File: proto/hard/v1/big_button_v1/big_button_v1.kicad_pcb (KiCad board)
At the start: 2 copper layers, 20 x 50 mm, 18 parts, among them J1 RJ12, J2 RJ12, J3 Conn_01x02, J4 Conn_01x02, SW1 SW_Push, U1 LM393, U2 PC817, U3 PC817

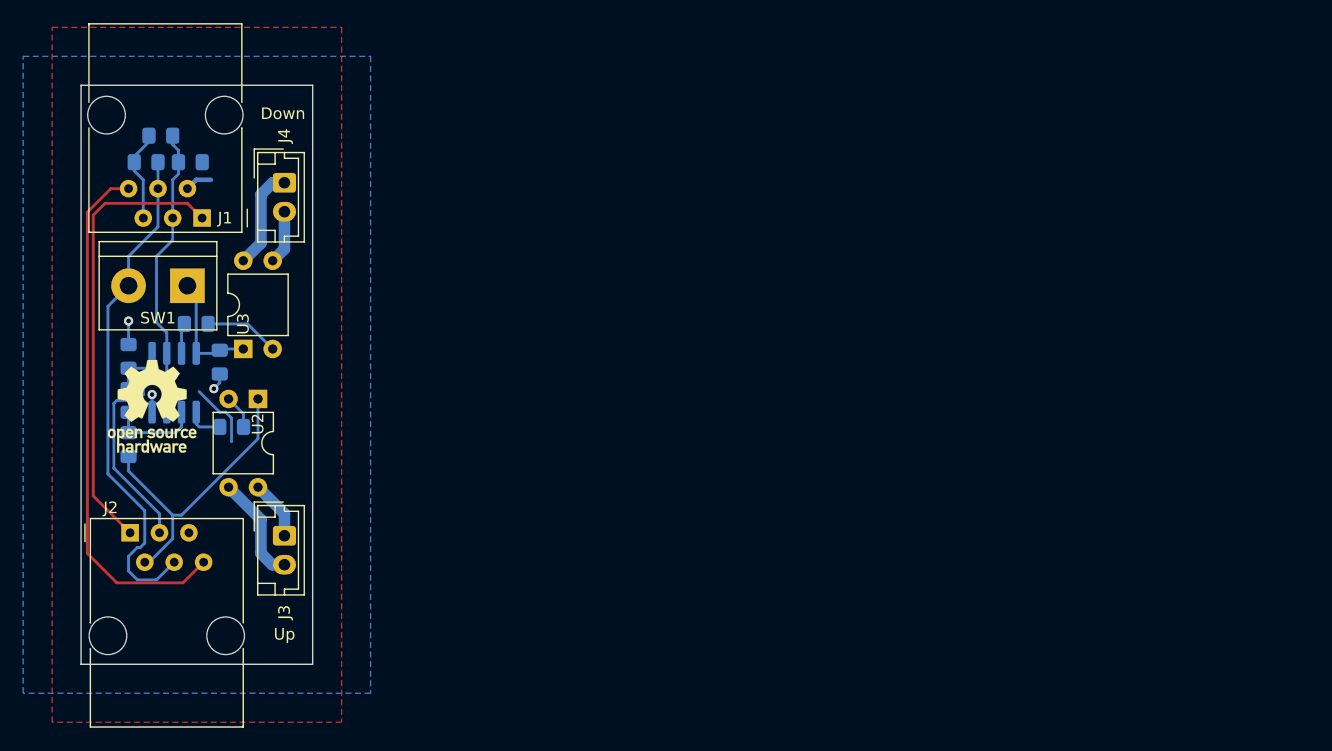
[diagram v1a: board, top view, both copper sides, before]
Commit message: Button rework - specialization for small case BMW50028. Includes button and single click LED highlight. Added diode to power line. Changed to single comparator.
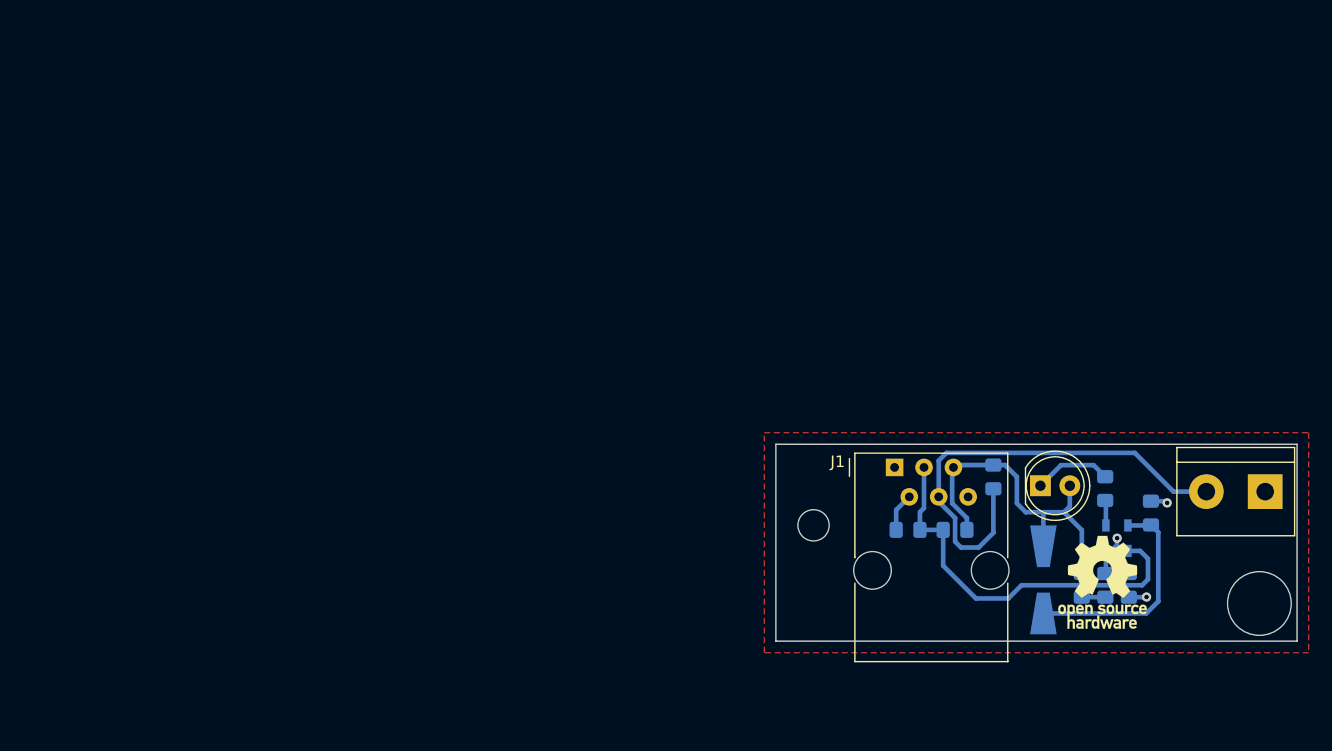
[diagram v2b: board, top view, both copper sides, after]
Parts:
- removed J2: RJ12, Connector_RJ:RJ12_Amphenol_54601
- removed J3, J4: Conn_01x02, Connector_JST:JST_EH_B2B-EH-A_1x02_P2.50mm_Vertical
- removed R8: 1k, Resistor_SMD:R_0805_2012Metric_Pad1.15x1.40mm_HandSolder
- removed U2, U3: PC817, Package_DIP:DIP-4_W7.62mm
- added D1: D_Schottky, Diode_SMD:D_SMA-SMB_Universal_Handsoldering, B.Cu at (133.1, 92.7)
- added D2: LED, LED_THT:LED_D5.0mm, F.Cu at (132.8, 84.6)
- added REF**: MountingHole_5.5mm, MountingHole:MountingHole_5.5mm, F.Cu at (151.8, 94.8)
- added REF**: MountingHole_2.7mm, MountingHole:MountingHole_2.7mm, F.Cu at (113.2, 88.0)
- U1: value LM393 -> MCP6566U; footprint Package_SO:SOP-8_3.76x4.96mm_P1.27mm -> Package_TO_SOT_SMD:SOT-23-5
- moved SW1 94.8 mm to (152.2, 85.1)
- moved R4 87.2 mm to (140.5, 93.2)
- moved R5 85.8 mm to (138.4, 93.2), turned to 270 degrees
- moved R6 84.7 mm to (136.4, 93.2)
- moved REF** 83.5 mm to (138.2, 92.9)
- moved U1 82.5 mm to (139.4, 89.1)
- moved C1 81.5 mm to (142.4, 86.9)
- moved R3 78.0 mm to (128.8, 83.8), turned to 90 degrees
- moved R2 76.6 mm to (125.5, 88.4), turned to 0 degrees
- moved R7 75.6 mm to (138.4, 84.8), turned to 90 degrees
- moved R1 69.6 mm to (121.4, 88.4), turned to 0 degrees
- moved J1 63.6 mm to (120.2, 83.0), turned to 0 degrees
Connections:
- C1 pad 1: VCC -> GND
- C1 pad 2: GND -> Net-(C1-Pad2)
- J1 pad 2: VCC -> GND
- J1 pad 5: GND -> VCC
- R1 pad 1: VCC -> GND
- R2 pad 2: GND -> VCC
- R3 pad 2: GND -> VCC
- R4 pad 1: VCC -> GND
- R6 pad 2: GND -> VCC
- R7 pad 2: /TopOut -> Net-(D2-Pad1)
- SW1 pad 1: VCC -> GND
- U1 pad 1: /TopOut -> /MiddlePoint
- U1 pad 2: Net-(R4-Pad2) -> GND
- U1 pad 3: /MiddlePoint -> Net-(R4-Pad2)
- U1 pad 4: GND -> Net-(R7-Pad1)
- U1 pad 5: Net-(R5-Pad2) -> Net-(C1-Pad2)
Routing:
- net Net-(J1-Pad6): track 45.7 -> 0.00 mm
- net Net-(J1-Pad1): track 39.1 -> 0.00 mm
- net Net-(C1-Pad2): track 0.00 -> 19.2 mm
- net VCC: track 44.0 -> 30.0 mm
- net /MiddlePoint: track 43.7 -> 34.0 mm
- net Net-(J3-Pad2): track 9.31 -> 0.00 mm
- net Net-(J4-Pad1): track 8.80 -> 0.00 mm
- net Net-(D2-Pad1): track 0.00 -> 6.74 mm
- net Net-(R8-Pad1): track 6.47 -> 0.00 mm
- net GND: track 13.0 -> 7.42 mm
- net Net-(J3-Pad1): track 5.14 -> 0.00 mm
- net Net-(J4-Pad2): track 4.65 -> 0.00 mm
- net Net-(J1-Pad4): track 44.0 -> 40.2 mm
- net Net-(R4-Pad2): track 7.81 -> 4.00 mm
- net /TopOut: track 3.16 -> 0.00 mm
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- removed copper zone on B.Cu, net VCC
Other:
- board size 20 x 50 mm -> 45 x 17 mm
- board text removed: "Down"
- board text removed: "Up"
